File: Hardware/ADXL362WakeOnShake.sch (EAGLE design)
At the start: 24 parts, among them J1 PROG_HDR, U1 ADXL362, U3 ADP160-3.3

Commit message: Added attribution for original concept.
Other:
- note added: "Original wake-on-shake concept by Nitzan Gadish, Analog Devices"
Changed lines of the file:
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@@
 <sheet>
 <plain>
-<text x="167.64" y="7.62" size="5.08" layer="94">Mike Hord</text>
+<text x="173.482" y="7.62" size="5.08" layer="94">Mike Hord</text>
 <text x="238.252" y="5.842" size="5.08" layer="94">10</text>
+<text x="2.54" y="2.54" size="1.778" layer="94">Original wake-on-shake concept by
+Nitzan Gadish, Analog Devices</text>
 </plain>
 <instances>
@@
 </schematic>
 </drawing>
+<compatibility>
+<note version="6.3" minversion="6.2.2" severity="warning">
+Since Version 6.2.2 text objects can contain more than one line,
+which will not be processed correctly with this version.
+</note>
+</compatibility>
 </eagle>

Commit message: Updated caps, res, sch, vers# and diodes
Updated caps/res to 0603  ,  1:1 on the adxl362, updated footprint for
diodes, new rev #
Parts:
- C1, C4: device SparkFun-Passives:CAP0402-CAP -> SparkFun-Capacitors:0.1UF-25V(+80/-20%)(0603)
- C2, C3: device SparkFun-Passives:CAP0402-CAP -> SparkFun-Capacitors:1.0UF-16V-10%(0603)
- D1: device SparkFun-DiscreteSemi:DIODE-SCHOTTKY -> SparkFun-DiscreteSemi:RB751
- R1, R2: device SparkFun-Passives:RESISTOR0402-RES -> SparkFun-Resistors:1MOHM1/10W1%(0603)
- R3, R4: device SparkFun-Passives:RESISTOR0402-RES -> SparkFun-Resistors:10K-1%RES-00824
- U1: device SparkFun-Sensors:ADXL362 -> SparkFun-Sensors:ADXL362ADXL362-1:1
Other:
- note added: "11"
- note added: "Revised by:Patrick Alberts"
- note removed: "10"
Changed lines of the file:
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@@
 <?xml version="1.0" encoding="utf-8"?>
 <!DOCTYPE eagle SYSTEM "eagle.dtd">
-<eagle version="6.3">
+<eagle version="6.4">
 <drawing>
 <settings>
@@
 <layer number="106" name="bPlate" color="7" fill="1" visible="no" active="yes"/>
 <layer number="107" name="Crop" color="7" fill="1" visible="no" active="yes"/>
+<layer number="108" name="tplace-old" color="10" fill="1" visible="no" active="yes"/>
+<layer number="109" name="ref-old" color="11" fill="1" visible="no" active="yes"/>
 <layer number="116" name="Patch_BOT" color="9" fill="4" visible="no" active="yes"/>
 <layer number="121" name="_tsilk" color="7" fill="1" visible="no" active="yes"/>
@@
 <attribute name="PROD_ID" value="TRANS-07913"/>
 </part>
-<part name="U1" library="SparkFun-Sensors" deviceset="ADXL362" device="" value="ADXL362"/>
+<part name="U1" library="SparkFun-Sensors" deviceset="ADXL362" device="ADXL362-1:1" value="ADXL362"/>
 <part name="FRAME1" library="SparkFun-Aesthetics" deviceset="FRAME-LETTER" device=""/>
 <part name="U$1" library="SparkFun-Aesthetics" deviceset="V_BATT" device=""/>
@@
 <attribute name="DIST_ID" value="ATTINY2313A-SU-ND"/>
 </part>
-<part name="R1" library="SparkFun-Passives" deviceset="RESISTOR" device="0402-RES" value="1M">
+<part name="R1" library="SparkFun-Resistors" deviceset="1MOHM1/10W1%(0603)" device="" value="1M">
 <attribute name="PROD_ID" value="RES-07868"/>
 </part>
-<part name="C1" library="SparkFun-Passives" deviceset="CAP" device="0402-CAP" value=".1uF">
+<part name="C1" library="SparkFun-Capacitors" deviceset="0.1UF-25V(+80/-20%)(0603)" device="" value=".1uF">
 <attribute name="PROD_ID" value="CAP-00810"/>
 </part>
-<part name="D1" library="SparkFun-DiscreteSemi" deviceset="DIODE-SCHOTTKY" device="" value="RB751">
+<part name="D1" library="SparkFun-DiscreteSemi" deviceset="RB751" device="" value="RB751">
 <attribute name="PROD_ID" value="DIO-11018"/>
 </part>
@@
 <attribute name="DIST_ID" value="ADP160AUJZ-3.3-R7TR-ND"/>
 </part>
-<part name="R2" library="SparkFun-Passives" deviceset="RESISTOR" device="0402-RES" value="1M">
+<part name="R2" library="SparkFun-Resistors" deviceset="1MOHM1/10W1%(0603)" device="" value="1M">
 <attribute name="PROD_ID" value="RES-07868"/>
 </part>
-<part name="C2" library="SparkFun-Passives" deviceset="CAP" device="0402-CAP" value="1uF">
+<part name="C2" library="SparkFun-Capacitors" deviceset="1.0UF-16V-10%(0603)" device="" value="1uF">
 <attribute name="PROD_ID" value="CAP-00868"/>
 </part>
-<part name="C3" library="SparkFun-Passives" deviceset="CAP" device="0402-CAP" value="1uF">
+<part name="C3" library="SparkFun-Capacitors" deviceset="1.0UF-16V-10%(0603)" device="" value="1uF">
 <attribute name="PROD_ID" value="CAP-00868"/>
 </part>
@@
 <part name="GND4" library="SparkFun-Aesthetics" deviceset="GND" device=""/>
 <part name="P+3" library="SparkFun-Aesthetics" deviceset="3.3V" device=""/>
-<part name="C4" library="SparkFun-Passives" deviceset="CAP" device="0402-CAP" value=".1uF">
+<part name="C4" library="SparkFun-Capacitors" deviceset="0.1UF-25V(+80/-20%)(0603)" device="" value=".1uF">
 <attribute name="PROD_ID" value="CAP-00810"/>
 </part>
@@
 <part name="GND6" library="SparkFun-Aesthetics" deviceset="GND" device=""/>
 <part name="P+5" library="SparkFun-Aesthetics" deviceset="3.3V" device=""/>
-<part name="R3" library="SparkFun-Passives" deviceset="RESISTOR" device="0402-RES" value="10k">
+<part name="R3" library="SparkFun-Resistors" deviceset="10K-1%" device="RES-00824" value="10k">
 <attribute name="PROD_ID" value="RES-00824"/>
 </part>
@@
 <part name="JP6" library="SparkFun-Aesthetics" deviceset="LOGO-SFE" device="NEW"/>
 <part name="JP7" library="SparkFun-Connectors" deviceset="M05" device="PTH"/>
-<part name="R4" library="SparkFun-Passives" deviceset="RESISTOR" device="0402-RES" value="10k">
+<part name="R4" library="SparkFun-Resistors" deviceset="10K-1%" device="RES-00824" value="10k">
 <attribute name="PROD_ID" value="RES-00824"/>
 </part>
@@
 <sheet>
 <plain>
-<text x="173.482" y="7.62" size="5.08" layer="94">Mike Hord</text>
-<text x="238.252" y="5.842" size="5.08" layer="94">10</text>
+<text x="165.608" y="11.43" size="2.54" layer="94">Mike Hord</text>
+<text x="238.252" y="5.842" size="5.08" layer="94">11</text>
 <text x="2.54" y="2.54" size="1.778" layer="94">Original wake-on-shake concept by
 Nitzan Gadish, Analog Devices</text>
+<text x="149.86" y="7.62" size="1.778" layer="94">Revised by:Patrick Alberts</text>
 </plain>
 <instances>

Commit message: Fixed FDTI ann rings / added standoff
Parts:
- removed U$3: OSHW-LOGOM, SparkFun-Aesthetics:OSHW-LOGOM
- JP2: value (none) -> M02-JST-2MM-SMT
- JP5: value (none) -> M02PTH
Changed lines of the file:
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@@
 <part name="GND7" library="SparkFun-Aesthetics" deviceset="GND" device=""/>
 <part name="JP4" library="SparkFun-Aesthetics" deviceset="LOGO-SFE" device="NW2"/>
-<part name="U$3" library="SparkFun-Aesthetics" deviceset="OSHW-LOGO" device="M"/>
 <part name="JP5" library="SparkFun-Connectors" deviceset="M02" device="PTH"/>
 <part name="JP6" library="SparkFun-Aesthetics" deviceset="LOGO-SFE" device="NEW"/>
@@
 <instance part="GND7" gate="1" x="60.96" y="20.32"/>
 <instance part="JP4" gate="G$1" x="241.3" y="17.78"/>
-<instance part="U$3" gate="G$1" x="233.68" y="48.26"/>
 <instance part="JP5" gate="G$1" x="30.48" y="68.58" rot="MR180"/>
 <instance part="JP6" gate="G$1" x="241.3" y="17.78"/>

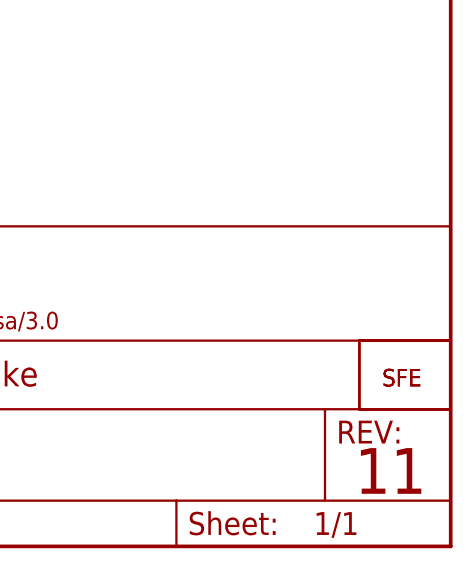
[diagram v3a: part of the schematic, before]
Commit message: added regular fiducials
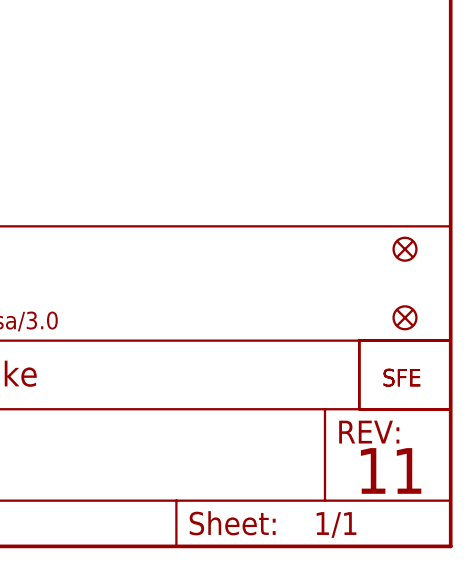
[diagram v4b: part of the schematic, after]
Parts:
- added FID1, FID2: FIDUCIAL1X2, SparkFun-Aesthetics:FIDUCIAL1X2
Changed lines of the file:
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@@
 <?xml version="1.0" encoding="utf-8"?>
 <!DOCTYPE eagle SYSTEM "eagle.dtd">
-<eagle version="6.4">
+<eagle version="6.5.0">
 <drawing>
 <settings>
@@
 </part>
 <part name="P+7" library="SparkFun-Aesthetics" deviceset="3.3V" device=""/>
+<part name="FID1" library="SparkFun-Aesthetics" deviceset="FIDUCIAL" device="1X2"/>
+<part name="FID2" library="SparkFun-Aesthetics" deviceset="FIDUCIAL" device="1X2"/>
 </parts>
 <sheets>
@@
 </instance>
 <instance part="P+7" gate="G$1" x="48.26" y="43.18"/>
+<instance part="FID1" gate="G$1" x="243.84" y="33.02"/>
+<instance part="FID2" gate="G$1" x="243.84" y="25.4"/>
 </instances>
 <busses>
